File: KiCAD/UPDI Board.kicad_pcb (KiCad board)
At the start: 2 copper layers, 19.1 x 30.5 mm, 18 parts, among them J1 AVR UPDI Header, J10 Primary Header, J12 Second Header, J13 RS485, J14 UART0, J15 UPDI, J16 Voltage in, J17 UART1, U7 MAX3072E

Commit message: .
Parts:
- moved JP3 1.91 mm to (170.2, 58.4)
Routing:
- net /RX1: track 28.1 -> 27.1 mm
- net /B: track 22.3 -> 21.6 mm
- net +Ve: track 44.1 -> 44.7 mm

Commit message: .
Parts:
- added C19: 220n, Capacitor_SMD:C_0805_2012Metric_Pad1.18x1.45mm_HandSolder, F.Cu at (182.2, 55.9)
- added R18: 10, Resistor_SMD:R_0805_2012Metric_Pad1.20x1.40mm_HandSolder, F.Cu at (170.4, 55.9)
- added R19: 10, Resistor_SMD:R_0805_2012Metric_Pad1.20x1.40mm_HandSolder, F.Cu at (178.4, 55.9)
- C18: value 100nF -> 100n
- moved J15 1.91 mm to (182.2, 52.1)
- moved R17 1.42 mm to (174.6, 55.9)
- moved J17 1.16 mm to (182.2, 48.9)
- moved J14 0.63 mm to (182.2, 45.7)
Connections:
- J13 pad 2: /A -> Net-(J13-Pin_2)
- J13 pad 3: /B -> Net-(J13-Pin_3)
- R17 pad 1: /B -> Net-(J13-Pin_3)
- R17 pad 2: /A -> Net-(J13-Pin_2)
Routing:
- net Net-(J13-Pin_2): track 0.00 -> 21.6 mm, vias 0 -> 1
- net GND: track 6.24 -> 26.5 mm
- net /A: track 25.5 -> 8.26 mm, vias 2 -> 0
- net Net-(J13-Pin_3): track 0.00 -> 15.9 mm, vias 0 -> 1
- net /B: track 21.6 -> 6.56 mm, vias 2 -> 0
- net +Ve: track 44.7 -> 55.9 mm
- net +5V: track 81.3 -> 76.6 mm, vias 1 -> 4
- net /RX0: track 43.1 -> 45.2 mm
- net +3V3: track 26.6 -> 24.5 mm
- net /RX1: track 27.1 -> 28.7 mm
- net /TX1: track 24.3 -> 25.1 mm
- net /UPDI: track 27.9 -> 27.8 mm, vias 0 -> 2

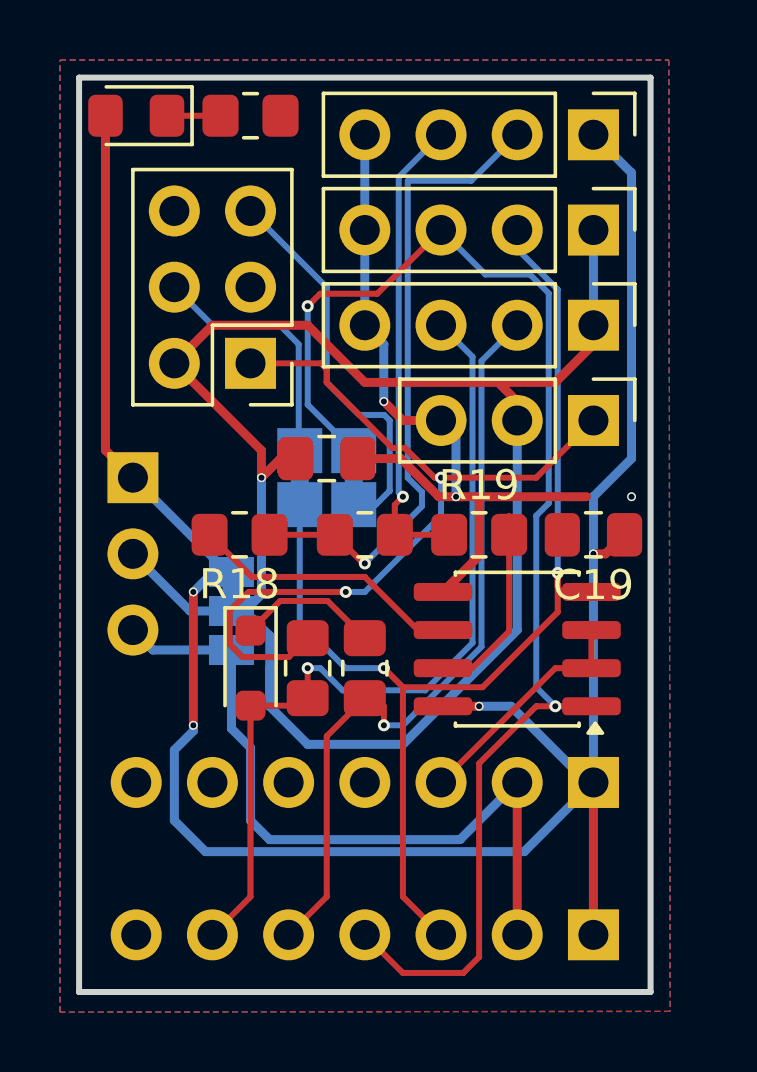
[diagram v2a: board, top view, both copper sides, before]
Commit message: added ground plane
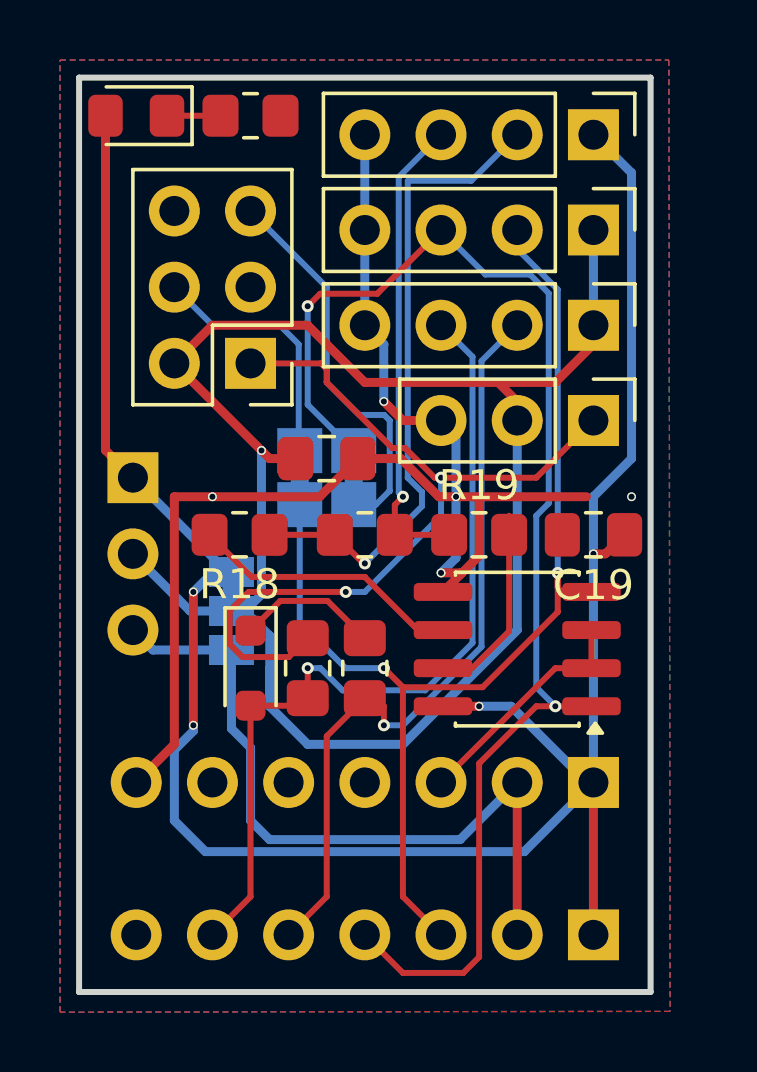
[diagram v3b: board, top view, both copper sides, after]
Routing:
- net GND: track 26.5 -> 46.0 mm, vias 3 -> 5

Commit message: .
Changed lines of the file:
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@@
 			(at 0 1.65 0)
 			(layer "F.Fab")
+			(hide yes)
 			(effects
 				(font
@@
 			(at 1.27 7.46 0)
 			(layer "F.Fab")
+			(hide yes)
 			(effects
 				(font
@@
 			(at 0 10 90)
 			(layer "F.Fab")
+			(hide yes)
 			(effects
 				(font
@@
 			(at 0 -1.65 0)
 			(layer "F.SilkS")
+			(hide yes)
 			(effects
 				(font
@@
 			(at 0 -1.68 0)
 			(layer "F.SilkS")
+			(hide yes)
 			(effects
 				(font
@@
 			(at 0 -1.65 0)
 			(layer "F.SilkS")
+			(hide yes)
 			(effects
 				(font
@@
 			(at 0 1.65 90)
 			(layer "F.Fab")
+			(hide yes)
 			(effects
 				(font
@@
 			(at 0 1.65 0)
 			(layer "F.Fab")
+			(hide yes)
 			(effects
 				(font
@@
 	)
 	(segment
-		(start 180.34 60.96)
-		(end 180.34 55.245)
+		(start 180.755 54.83)
+		(end 180.755 47.829264)
 		(width 0.2)
 		(layer "B.Cu")
@@
 	)
 	(segment
-		(start 172.72 48.26)
-		(end 172.72 51.54)
+		(start 178.647132 47.202132)
+		(end 177.165 45.72)
 		(width 0.2)
 		(layer "B.Cu")
@@
 	)
 	(segment
-		(start 178.647132 47.202132)
-		(end 177.165 45.72)
+		(start 180.34 60.96)
+		(end 180.34 55.245)
 		(width 0.2)
 		(layer "B.Cu")
@@
 	)
 	(segment
-		(start 180.975 61.595)
-		(end 180.34 60.96)
+		(start 173.055 50.924264)
+		(end 173.99 51.859264)
 		(width 0.2)
 		(layer "B.Cu")
@@
 	)
 	(segment
-		(start 180.755 54.83)
-		(end 180.755 47.829264)
+		(start 173.99 51.859264)
+		(end 173.99 52.81)
 		(width 0.2)
 		(layer "B.Cu")
@@
 	)
 	(segment
-		(start 180.34 55.245)
-		(end 180.755 54.83)
+		(start 180.127868 47.202132)
+		(end 178.647132 47.202132)
 		(width 0.2)
 		(layer "B.Cu")
@@
 	)
 	(segment
-		(start 172.72 51.54)
-		(end 174.255 53.075)
+		(start 180.975 61.595)
+		(end 180.34 60.96)
 		(width 0.2)
 		(layer "B.Cu")
@@
 	)
 	(segment
-		(start 180.127868 47.202132)
-		(end 178.647132 47.202132)
+		(start 172.72 48.26)
+		(end 173.055 48.595)
+		(width 0.2)
+		(layer "B.Cu")
+		(net "/RX0")
+	)
+	(segment
+		(start 173.055 48.595)
+		(end 173.055 50.924264)
+		(width 0.2)
+		(layer "B.Cu")
+		(net "/RX0")
+	)
+	(segment
+		(start 180.34 55.245)
+		(end 180.755 54.83)
+		(width 0.2)
+		(layer "B.Cu")
+		(net "/RX0")
+	)
+	(segment
+		(start 173.99 52.81)
+		(end 174.255 53.075)
 		(width 0.2)
 		(layer "B.Cu")
@@
 	)
 	(segment
-		(start 172.455 53.075)
-		(end 172.42 53.04)
+		(start 172.72 49.3625)
+		(end 172.2525 48.895)
 		(width 0.2)
 		(layer "B.Cu")
@@
 	)
 	(segment
-		(start 169.545 48.895)
-		(end 168.275 47.625)
+		(start 172.455 53.075)
+		(end 172.72 52.81)
 		(width 0.2)
 		(layer "B.Cu")
@@
 	)
 	(segment
-		(start 172.42 53.04)
-		(end 172.42 49.53)
+		(start 169.545 48.895)
+		(end 168.275 47.625)
 		(width 0.2)
 		(layer "B.Cu")
@@
 	)
 	(segment
-		(start 171.785 48.895)
-		(end 169.545 48.895)
+		(start 172.72 52.81)
+		(end 172.72 49.3625)
 		(width 0.2)
 		(layer "B.Cu")
@@
 	)
 	(segment
-		(start 172.42 49.53)
-		(end 171.785 48.895)
+		(start 172.2525 48.895)
+		(end 169.545 48.895)
 		(width 0.2)
 		(layer "B.Cu")
@@
 	)
 	(segment
-		(start 176.53 54.93)
-		(end 176.53 54.45)
+		(start 176.53 54.45)
+		(end 176.53 54.93)
 		(width 0.2)
 		(layer "B.Cu")
@@
 	)
 	(segment
-		(start 174.625 56.835)
-		(end 176.53 54.93)
+		(start 176.425736 44.079264)
+		(end 176.055 44.45)
 		(width 0.2)
 		(layer "B.Cu")
@@
 	)
 	(segment
-		(start 176.53 54.45)
-		(end 176.055 53.975)
+		(start 176.055 53.975)
+		(end 176.53 54.45)
+		(width 0.2)
+		(layer "B.Cu")
+		(net "Net-(J13-Pin_2)")
+	)
+	(segment
+		(start 176.53 54.93)
+		(end 174.625 56.835)
 		(width 0.2)
 		(layer "B.Cu")
@@
 	(segment
 		(start 178.170736 44.079264)
-		(end 179.705 42.545)
+		(end 176.425736 44.079264)
 		(width 0.2)
 		(layer "B.Cu")
@@
 	)
 	(segment
-		(start 176.055 53.975)
-		(end 176.055 44.079264)
+		(start 176.055 44.45)
+		(end 176.055 53.975)
 		(width 0.2)
 		(layer "B.Cu")
@@
 	)
 	(segment
-		(start 176.055 44.079264)
+		(start 179.705 42.545)
 		(end 178.170736 44.079264)
 		(width 0.2)

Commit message: .
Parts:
- moved C18 3.17 mm to (170.2, 53.3)
- moved J1 1.27 mm to (169.5, 50.2)
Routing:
- net GND: track 46.0 -> 14.8 mm, vias 5 -> 1
- net +Ve: track 56.3 -> 38.3 mm, vias 1 -> 0
- net +3V3: track 24.5 -> 29.4 mm
- net +5V: track 76.6 -> 80.2 mm, vias 4 -> 2
- net /RX1: track 28.7 -> 25.3 mm
- net /UPDI: track 27.8 -> 30.5 mm
- net /RX0: track 45.2 -> 43.0 mm
- net /TX1: track 25.1 -> 23.1 mm
